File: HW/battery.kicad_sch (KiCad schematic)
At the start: 0 parts

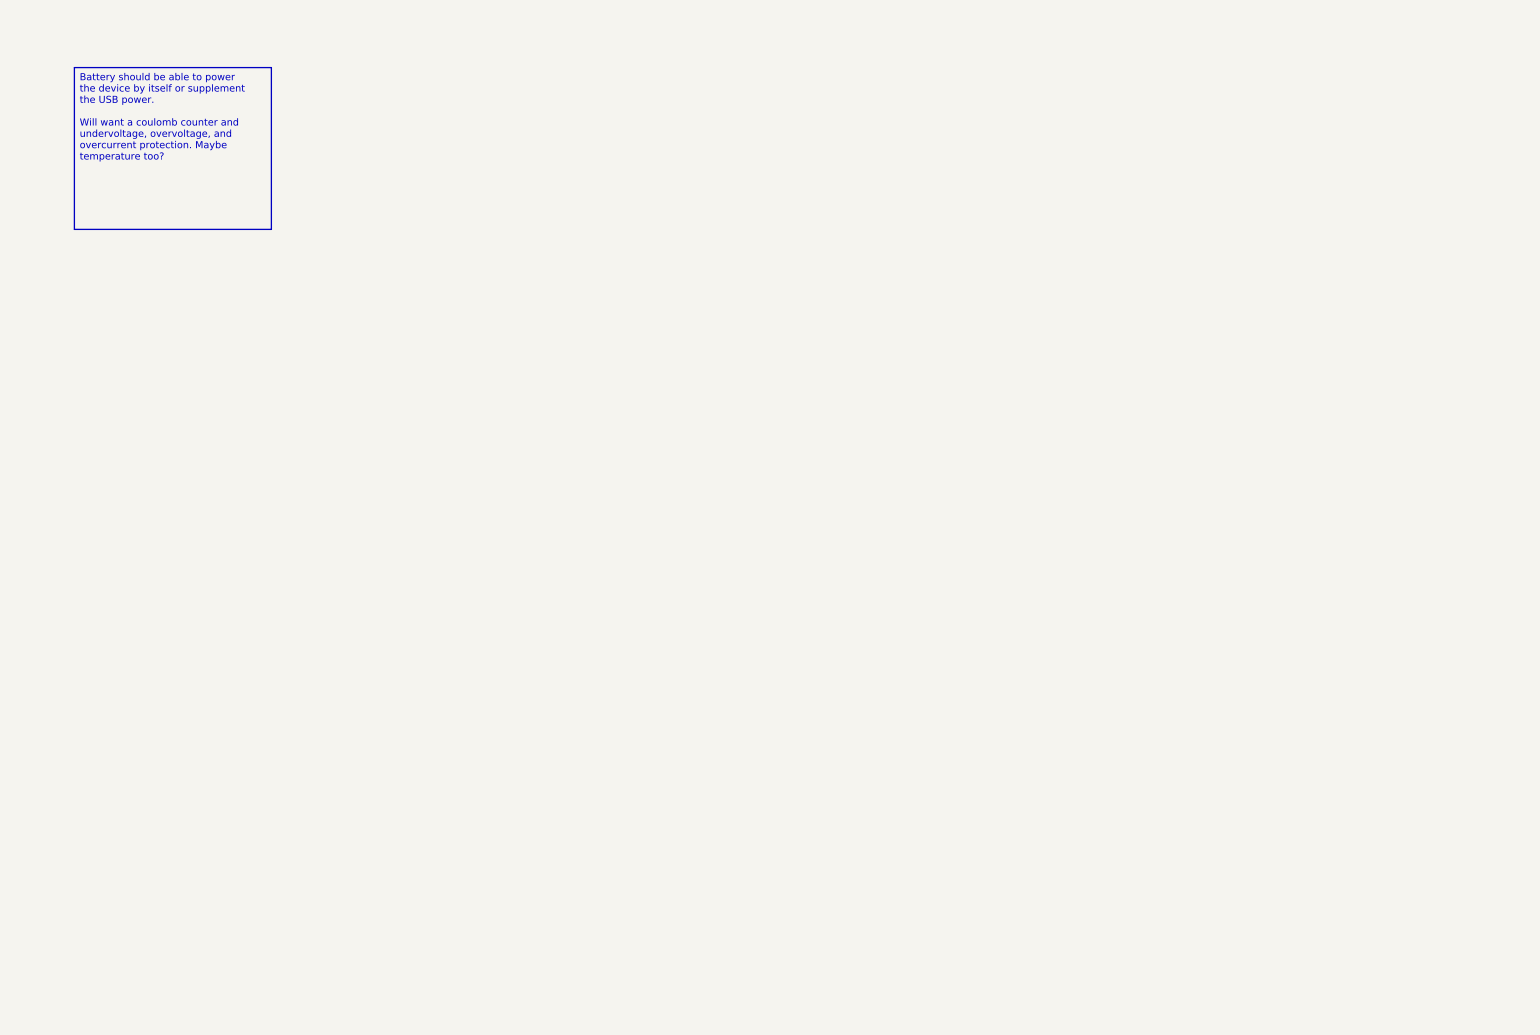
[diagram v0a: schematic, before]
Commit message: Almost first schematic draft (missing resistor values for STDRIVE current sensing and leds)
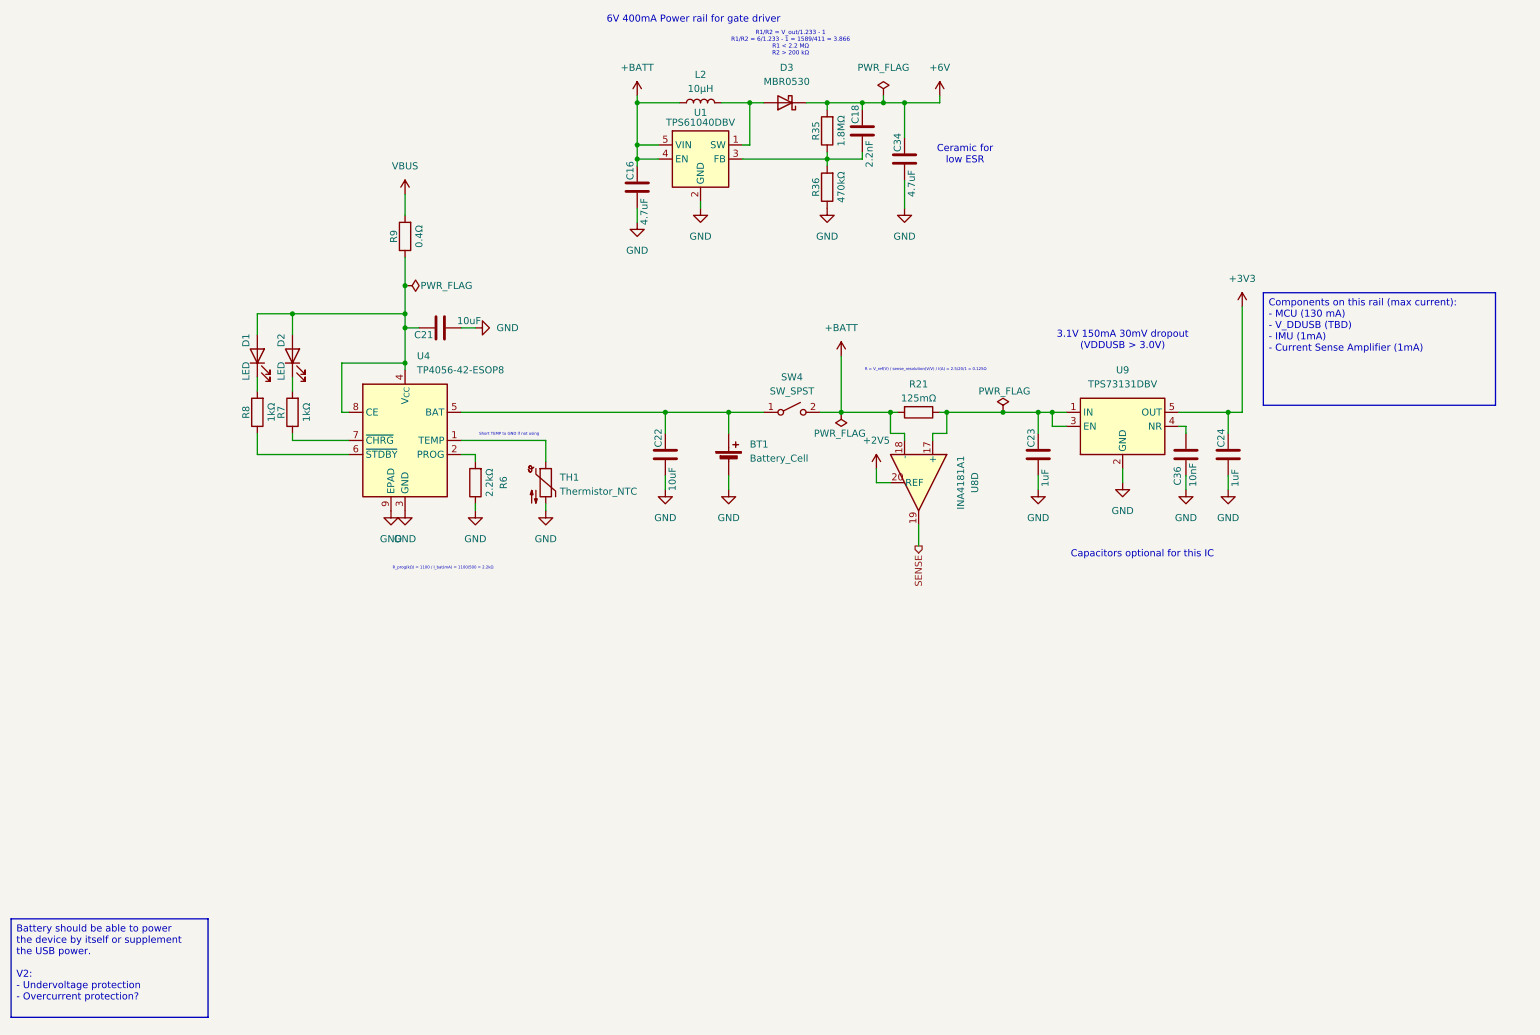
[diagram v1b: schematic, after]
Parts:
- added BT1: Battery_Cell, symbol Device:Battery_Cell
- added C16, C34: 4.7uF, Capacitor_SMD:C_0805_2012Metric, symbol Device:C
- added C18: 2.2nF, Capacitor_SMD:C_0402_1005Metric, symbol Device:C
- added C21, C22: 10uF, Capacitor_SMD:C_0402_1005Metric, symbol Device:C
- added C23, C24: 1uF, Capacitor_SMD:C_0402_1005Metric, symbol Device:C
- added C36: 10nF, Capacitor_SMD:C_0402_1005Metric, symbol Device:C
- added D1, D2: LED, symbol Device:LED
- added D3: MBR0530, Diode_SMD:D_SOD-123, symbol Diode:MBR0530
- added L2: 10μH, symbol Device:L
- added R21: 125mΩ, Resistor_SMD:R_0402_1005Metric, symbol Device:R
- added R35: 1.8MΩ, Resistor_SMD:R_0402_1005Metric, symbol Device:R
- added R36: 470kΩ, Resistor_SMD:R_0402_1005Metric, symbol Device:R
- added R6: 2.2kΩ, Resistor_SMD:R_0402_1005Metric, symbol Device:R
- added R7, R8: 1kΩ, Resistor_SMD:R_0402_1005Metric, symbol Device:R
- added R9: 0.4Ω, Resistor_SMD:R_0402_1005Metric, symbol Device:R
- added SW4: SW_SPST, symbol Switch:SW_SPST
- added TH1: Thermistor_NTC, symbol Device:Thermistor_NTC
- added U1: TPS61040DBV, Package_TO_SOT_SMD:SOT-23-5, symbol Regulator_Switching:TPS61040DBV
- added U4: TP4056-42-ESOP8, Package_SO:SOIC-8-1EP_3.9x4.9mm_P1.27mm_EP2.41x3.3mm_ThermalVias, symbol Battery_Management:TP4056-42-ESOP8
- added U8: INA4181A1, Package_SO:TSSOP-20_4.4x6.5mm_P0.65mm, symbol lib:INA4181A1
- added U9: TPS73131DBV, Package_TO_SOT_SMD:SOT-23-5, symbol Regulator_Linear:TPS73131DBV
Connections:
- new net: C18.2, R35.1, R36.2, U1.3 (FB)
- new net: D3.2 (A), L2.2, U1.1 (SW)
- new net: C21.1, D1.2 (A), D2.2 (A), R9.1, U4.4 (V_{CC}), U4.8 (CE)
- new net: C23.1, R21.1, U8.17 (+), U9.1 (IN), U9.3 (EN)
- new net: C36.1, U9.4 (NR)
- new net: TH1.1, U4.1 (TEMP)
- new net: R6.2, U4.2 (PROG)
- new net: BT1.1 (+), C22.1, SW4.1 (A), U4.5 (BAT)
- new net: R8.1, U4.6 (~{STDBY})
- new net: R7.1, U4.7 (~{CHRG})
- new net: D1.1 (K), R8.2
- new net: D2.1 (K), R7.2
- new net +2V5: U8.20 (REF)
- new net +3V3: C24.1, U9.5 (OUT)
- new net +6V: C18.1, C34.1, D3.1 (K), R35.2
- new net +BATT: C16.1, L2.1, R21.2, SW4.2 (B), U1.4 (EN), U1.5 (VIN), U8.18 (-)
- new net GND: BT1.2 (-), C16.2, C21.2, C22.2, C23.2, C24.2, C34.2, C36.2, R36.1, R6.1, TH1.2, U1.2 (GND), U4.3 (GND), U4.9 (EPAD), U9.2 (GND)
- new net SENSE: U8.19
- new net VBUS: R9.2
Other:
- note added: "3.1V 150mA 30mV dropout (VDDUSB > 3.0V)"
- note added: "6V 400mA Power rail for gate driver"
- note added: "Capacitors optional for this IC"
- note added: "Ceramic for low ESR"
- note added: "R = V_ref(V) / sense_resolution(V/V) / I(A) = 2.5/20/1 = 0.125Ω"
- note added: "R1/R2 = V_out/1.233 - 1 R1/R2 = 6/1.233 - 1 = 1589/411 = 3.866 R1 < 2.2 MΩ R2 > 200 kΩ"
- note added: "R_prog(kΩ) = 1100 / I_bat(mA) = 1100/500 = 2.2kΩ"
- note added: "Short TEMP to GND if not using"

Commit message: Cleaned up and implemented some of Laimonas' feedback
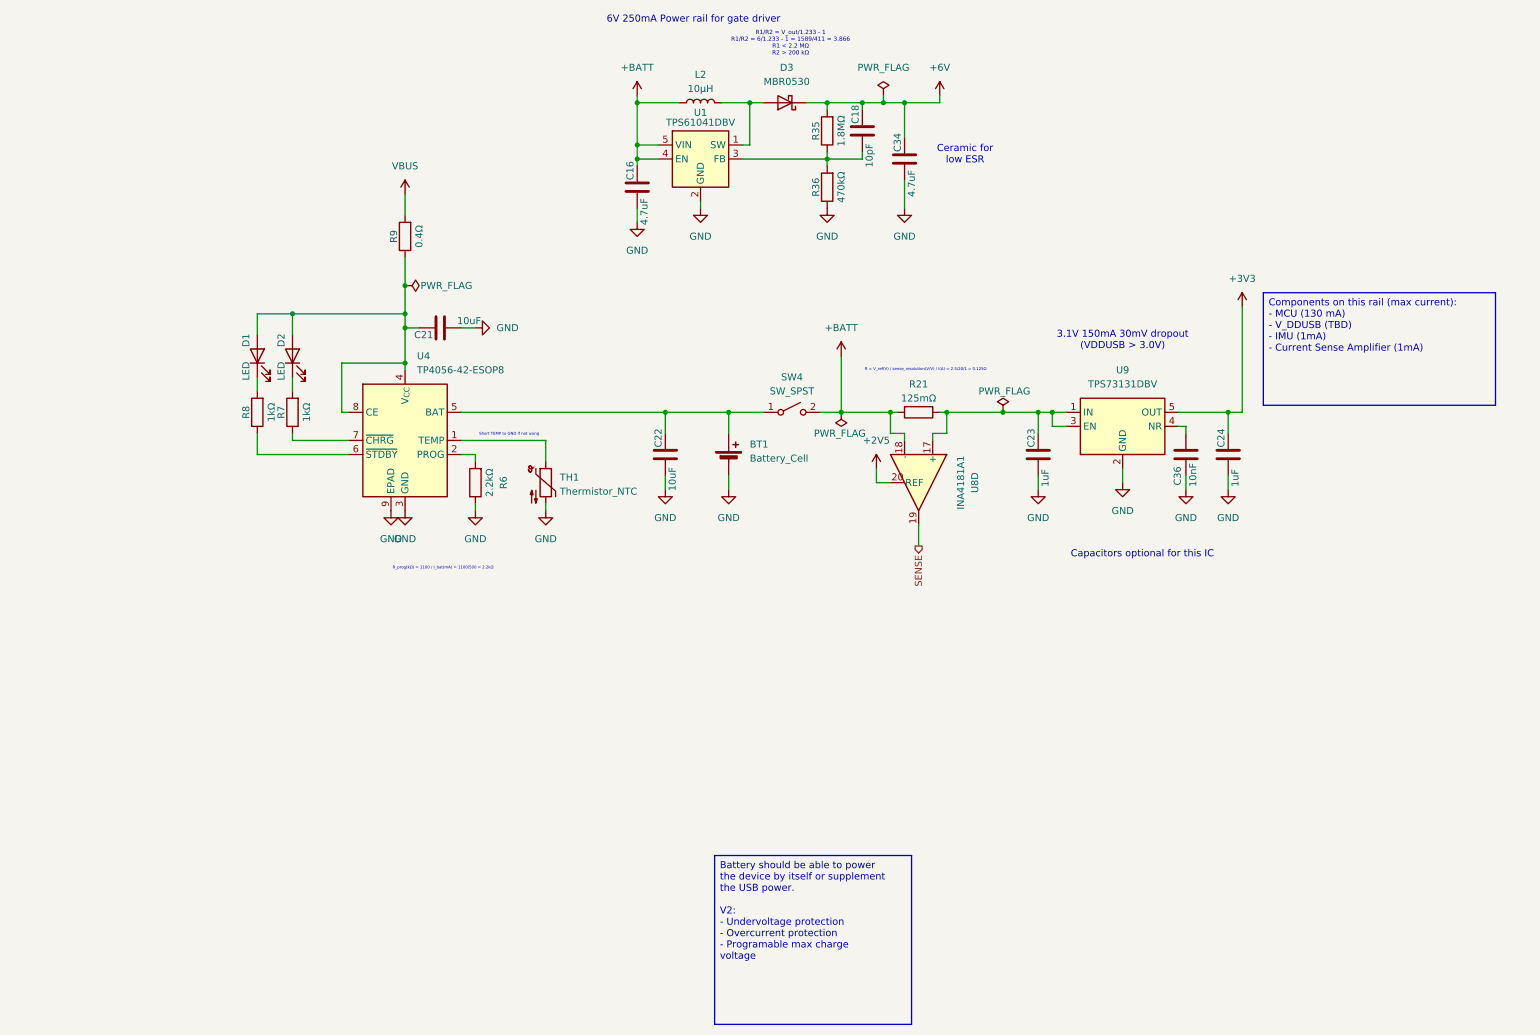
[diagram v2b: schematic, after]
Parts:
- C18: value 2.2nF -> 10pF
- U1: value TPS61040DBV -> TPS61041DBV
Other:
- note added: "6V 250mA Power rail for gate driver"
- note removed: "6V 400mA Power rail for gate driver"
- company: (none) -> Roberto Holmes
- title: (none) -> Capstan
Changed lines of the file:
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@@
 	(generator_version "9.0")
 	(paper "A4")
-	(text "6V 400mA Power rail for gate driver"
+	(title_block
+		(title "Capstan")
+		(date "2025-09-26")
+		(company "Roberto Holmes")
+	)
+	(text "6V 250mA Power rail for gate driver"
 		(exclude_from_sim no)
 		(at 137.16 15.494 0)
@@
 		)
 	)
-	(text_box "Battery should be able to power the device by itself or supplement the USB power.\n\nV2:\n- Undervoltage protection\n- Overcurrent protection?"
+	(text_box "Battery should be able to power the device by itself or supplement the USB power.\n\nV2:\n- Undervoltage protection\n- Overcurrent protection\n- Programable max charge voltage"
 		(exclude_from_sim no)
-		(at 13.97 177.8 0)
-		(size 35.56 17.78)
+		(at 140.97 166.37 0)
+		(size 35.56 30.48)
 		(margins 0.9525 0.9525 0.9525 0.9525)
 		(stroke
@@
 			)
 		)
-		(property "Value" "TPS61040DBV"
+		(property "Value" "TPS61041DBV"
 			(at 138.43 34.036 0)
 			(effects
@@
 			)
 		)
-		(property "Value" "2.2nF"
+		(property "Value" "10pF"
 			(at 168.91 42.164 90)
 			(effects
@@
 			)
 		)
-		(property "Datasheet" "http://www.mccsemi.com/up_pdf/MBR0520~MBR0580(SOD123).pdf"
+		(property "Datasheet" "https://www.onsemi.com/pdf/datasheet/mbr0530-d.pdf"
 			(at 153.67 30.48 0)
 			(effects
